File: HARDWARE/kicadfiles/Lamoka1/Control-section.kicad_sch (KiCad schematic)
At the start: 59 parts, among them SW1 PTS636 SM43J SMTR LFS, U1 RP2354A, U2 AMS1117-3.3, U3 74AHCT1G125, U7 TPS62160DSGR, U8 TMP235A2DBZR, X1 ABM8-272-T3

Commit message: MPN fixes, footprint fixes, ADD MUX and voltage sensing. ADD photo in main readme
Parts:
- added C26: 1uF, symbol Device:C
- added C27, C28, C29, C30: 47nF, symbol Device:C
- added R23, R24: 4.7k, symbol Device:R
- added R25: 36.5k, symbol Device:R
- added R26, R28, R30, R32: 10k, symbol Device:R
- added R27: 43.2k, symbol Device:R
- added R29, R31: 45.3k, symbol Device:R
- added U10: ADS7128IRTER, ADS7128IRTER:WQFN16_RTE_TEX, symbol ADS7128IRTER:ADS7128IRTER
- C1, C10, C17, C18, C19, C2, C3, C4, C5, C6, C7, C8, C9: footprint components:CAP_0402_SAM -> 0; Manufacturer Samsung Electro-Mechanics -> 0
- C24: footprint CAP_TMK212_TAY -> TMK212BBJ106KG:CAP_TMK212_TAY; MPN (none) -> TMK212BBJ106KG
- C25: footprint G-31_MUR -> GRM31CR71A226KE15L:G-31_MUR; MPN (none) -> GRM31CR71A226KE15L
- CR1, CR2: value SS14-E3/61T -> 40V 1A Schottky; footprint DO-214AC_VIS -> SS14-E3/61T:DO-214AC_VIS; MPN (none) -> SS14-E3/61T
- D1, D10, D2, D3, D4, D5, D6, D7, D8, D9: MPN TZ-5050S2RGB-5V-I4-H1 -> WS2812B
- L3: footprint IND_PA4332.222NLT_PUL -> PA4332.222NLT:IND_PA4332.222NLT_PUL; MPN (none) -> PA4332.222NLT
- R19: footprint RC0603N_YAG -> RC0603FR-07180KL:RC0603N_YAG; MPN (none) -> RC0603FR-07180KL
- R20: footprint RC0402N_VIS -> CRCW0402953KFKED:RC0402N_VIS; MPN (none) -> CRCW0402953KFKED
- R21: footprint RES_CRCW_0402_VIS -> CRCW0402100KFKED:RES_CRCW_0402_VIS; MPN (none) -> CRCW0402100KFKED
- R22: footprint DBZ0003A-IPC_A -> TMP235A2DBZR:DBZ0003A-IPC_A
- U1: MPN SC1511-A4 -> RP2354A
- U7: footprint DSG8_1P6X0P9 -> TPS62160DSGR:DSG8_1P6X0P9; MPN (none) -> TPS62160DSGR
- U8: footprint DBZ0003A-IPC_A -> TMP235A2DBZR:DBZ0003A-IPC_A; MPN (none) -> TMP235A2DBZR
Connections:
- net 11-14v input: now also R25.1
- net 3v3: now also R23.1, R24.1, U10.10 (DVDD), U10.7 (AVDD)
- net GND: now also C26.2, C27.2, C28.2, C29.2, C30.2, R26.2, R28.2, R30.2, R32.2, U10.17 (GND), U10.9 (GND)
- net GPIO8: now reaches U1.12 (GPIO8)
- net GPIO8: now also R23.2, U10.14 (SDA)
- net GPIO9: now reaches U1.13 (GPIO9)
- net GPIO9: now also R24.2, U10.13 (SCL)
- new net: C26.1, U10.8 (DECAP)
- new net 17v: R27.1
- new net AIN0: C27.1, R25.2, R26.1, U10.15 (AIN0/GPIO0)
- new net AIN1: C28.1, R27.2, R28.1, U10.16 (AIN1/GPIO1)
- new net AIN2: C29.1, R29.2, R30.1, U10.1 (AIN2/GPIO2)
- new net AIN3: C30.1, R31.2, R32.1, U10.2 (AIN3/GPIO3)
- new net SW_A: R29.1
- new net SW_B: R31.1
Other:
- note added: "Input-rail-voltage"
- note added: "Left-Leg-H-Bridge"
- note added: "Output-of-17v-boost"
- note added: "Right-Leg-H-Bridge"
- moved on the sheet: C1, C10, C11, C2, C24, C25, C3, C4, C5, C6, C7, C8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

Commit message: ADD source current monitoring, and other features, some more correcting of MPN and footprints
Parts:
- added C31: 100nF, symbol Device:C
- added IC1: INA240A2DR, INA240A2DR:SOIC127P600X175-8N, symbol INA240A2DR:INA240A2DR
- added R33: 22, symbol Device:R
- U10: MPN (none) -> ADS7128IRTER
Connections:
- net 3v3: now also IC1.6 (VS)
- net GND: now also C31.2, IC1.2 (GND), IC1.3 (REF2), IC1.7 (REF1)
- net AIN4: now reaches U10.3 (AIN4/GPIO4)
- net AIN4: now also C31.1, R33.2
- new net: IC1.5 (OUT), R33.1
- new net RCS1-L: IC1.1 (IN-)
- new net RCS1-S: IC1.8 (IN+)
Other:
- note added: "Source-Current-Sensing"

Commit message: General work on schem, BOM, footprints. Rout 11-14v to 5v buck converter
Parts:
- C1, C10, C17, C18, C19, C2, C3, C4, C5, C6, C7, C8, C9: footprint 0 -> (none); Manufacturer 0 -> (none)
- C11: Manufacturer Murata Electronics -> (none)
- C12, C13, C14, C15, C16: Manufacturer Samsung Electro-Mechanics -> (none)
- C20, C21: Manufacturer FH -> (none)
- C24: value TMK212BBJ106KG -> 10uF; footprint TMK212BBJ106KG:CAP_TMK212_TAY -> TMK212BBJ106KG-T:CAPC2114X145N; MPN TMK212BBJ106KG -> TMK212BBJ106KG-T
- C25: value GRM31CR71A226KE15L -> 22uF; footprint GRM31CR71A226KE15L:G-31_MUR -> (none)
- D1, D10, D2, D3, D4, D5, D6, D7, D8, D9: Manufacturer TUOZHAN -> (none)
- IC1: Arrow Part Number INA240A2DR -> (none); Arrow Price/Stock https://www.arrow.com/en/products/ina240a2dr/texas-instrume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 -> (none); Height 1.75 -> (none); Manufacturer_Name Texas Instruments -> (none); Manufacturer_Part_Number INA240A2DR -> (none); Mouser Part Number 595-INA240A2DR -> (none); Mouser Price/Stock https://www.mouser.co.uk/ProductDetail/Texas-Instruments/IN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 -> (none)
- L1: Manufacturer Abracon -> (none)
- L3: value PA4332.222NLT -> 2.2uH, 4.3A; footprint PA4332.222NLT:IND_PA4332.222NLT_PUL -> (none)
- R1, R11, R2, R3, R4, R5, R6, R7, R8, R9: Manufacturer YAGEO -> (none)
- R19: value RC0603FR-07180KL -> 180k; footprint RC0603FR-07180KL:RC0603N_YAG -> (none)
- R20: value CRCW0402953KFKED -> 953k; footprint CRCW0402953KFKED:RC0402N_VIS -> (none)
- R21: value CRCW0402100KFKED -> 100k; footprint CRCW0402100KFKED:RES_CRCW_0402_VIS -> (none)
- SW1: Manufacturer C&K -> (none)
- U1: Manufacturer Raspberry Pi -> (none)
- U2: Manufacturer EVVO -> (none); Notes Exact EVVO AMS1117-3.3 stability requirement must be verifi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 -> (none)
- U3: Manufacturer Texas Instruments -> (none)
- X1: Manufacturer Abracon LLC -> (none)
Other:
- moved on the sheet: C24

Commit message: Improving documentation, some more routing
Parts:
- removed SW1: PTS636 SM43J SMTR LFS, components:SW_PTS636_CNK, symbol 2026-07-07_01-19-01:PTS636_SM43J_SMTR_LFS
- added SW1: B3F-4055, B3F-4055:SW_B3F-4050_OMR, symbol B3F-4055:B3F-4055
- C1, C10, C2, C3, C4, C5, C6, C7, C8, C9: footprint (none) -> Capacitor_SMD:C_0603_1608Metric
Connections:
- net BTN: now also SW1.1, SW1.2
- net GND: now also SW1.3, SW1.4
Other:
- moved on the sheet: R9

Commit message: ADD seperate user interface board, improve doccumentation
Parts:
- removed C1, C10, C2, C3, C4, C5, C6, C7, C8, C9: 100n, Capacitor_SMD:C_0603_1608Metric, symbol Device:C
- removed C11: 100u, Capacitor_SMD:C_1206_3216Metric, symbol Device:C
- removed D1, D10, D2, D3, D4, D5, D6, D7, D8, D9: WS2812B, LED_SMD:LED_WS2812B_PLCC4_5.0x5.0mm_P3.2mm, symbol LED:WS2812B
- removed R1: 330, Resistor_SMD:R_0603_1608Metric, symbol Device:R
- removed R9: 10k, components:RES_CRCW_0603, symbol Device:R
- removed SW1: B3F-4055, B3F-4055:SW_B3F-4050_OMR, symbol B3F-4055:B3F-4055
- removed U3: 74AHCT1G125, Package_TO_SOT_SMD:SOT-23-5, symbol 74xGxx:74AHCT1G125
- C12, C13: footprint components:CAP_CL_05_SAM -> Capacitor_SMD:C_0402_1005Metric
- C31: footprint (none) -> Capacitor_SMD:C_0603_1608Metric
- R2, R3: footprint components:RC0603N_YAG -> RC0603FR-07180KL:RC0603N_YAG
- R22: footprint TMP235A2DBZR:DBZ0003A-IPC_A -> (none)
- R33: footprint (none) -> Resistor_SMD:R_0603_1608Metric
- U2: footprint components:SOT-223_UMW -> Package_TO_SOT_SMD:SOT-223-3_TabPin2
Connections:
- no-connect marks 28 -> 27
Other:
- note added: "Pull-up for Fan tach"
- moved on the sheet: C26, C27, C28, C29, C30, C31, IC1, R22, R23, R24, R25, R26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

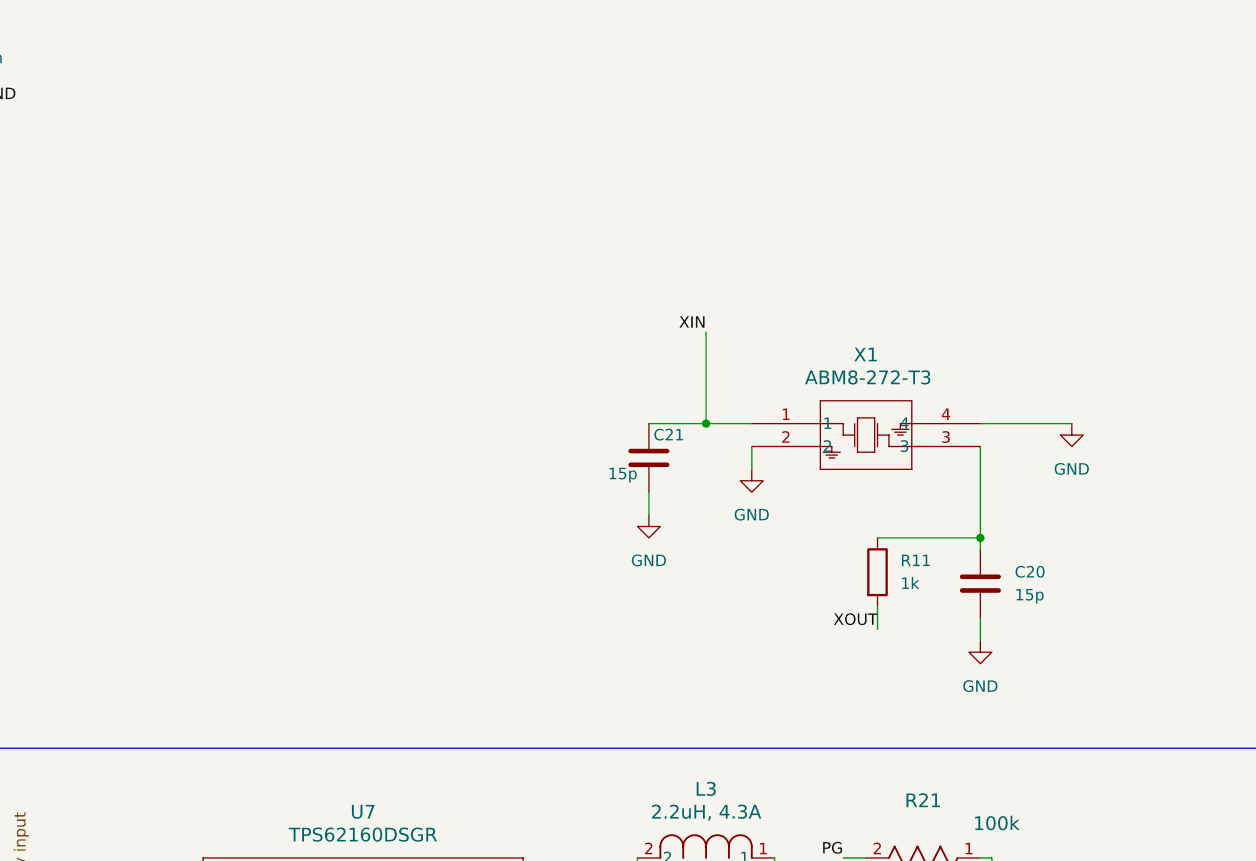
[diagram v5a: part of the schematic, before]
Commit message: Route in pin header for user interface board, and put in connector for fan, other changes as well
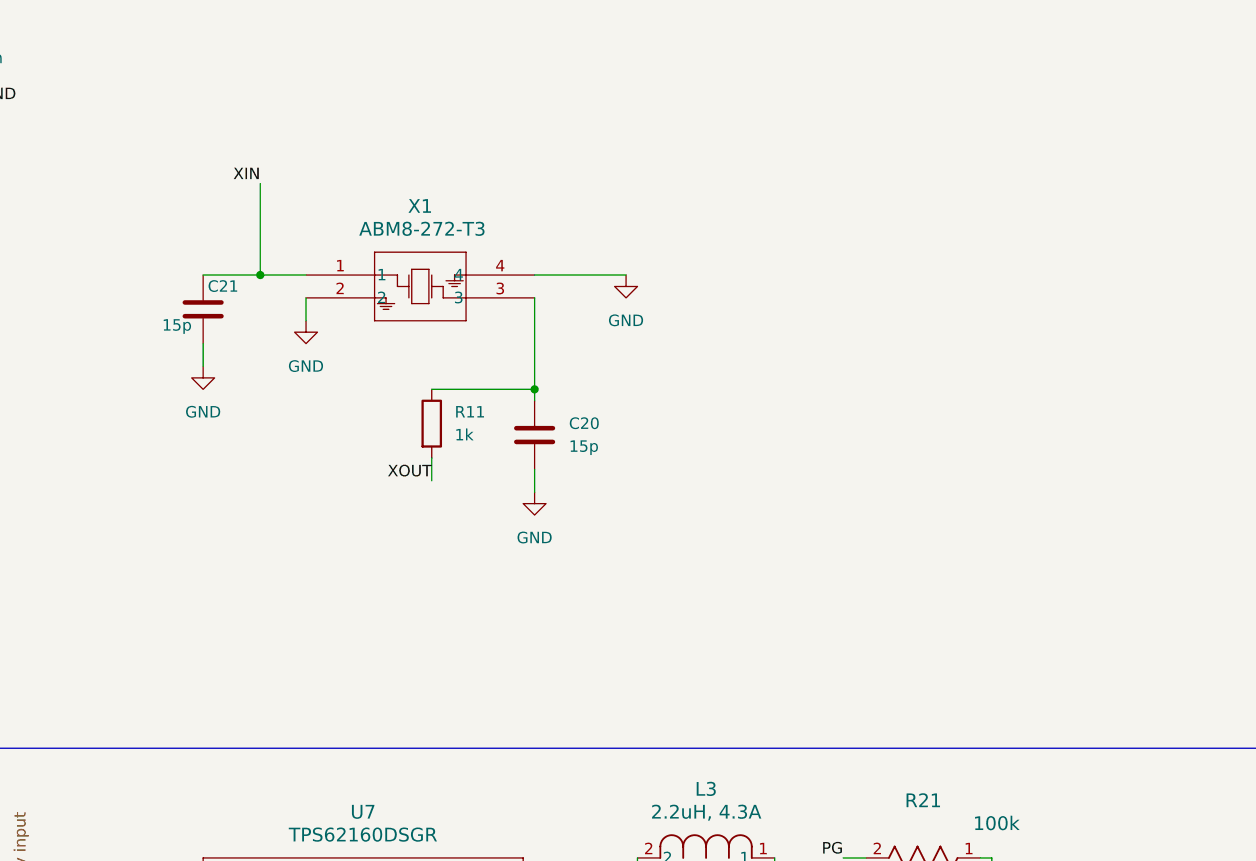
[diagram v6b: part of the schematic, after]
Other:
- moved on the sheet: C20, C21, R11, X1
